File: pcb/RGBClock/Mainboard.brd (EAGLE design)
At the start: 99.8 x 70.1 mm, 106 parts, among them IC1 MCP23017SO, IC2 LT1763CS8-1.5, K1 G6K-2F, K2 G6K-2F, K3 G6K-2F, K4 G6K-2F, Q1 32.768KHz, U1 MAX6369KA+T, U10 NX3L1G384GW, U11 NX3L1G384GW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

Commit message: dab routed
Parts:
- moved C23 1.98 mm to (61.1, 17.5), flipped to the top, turned to 180 degrees
- moved C24 1.37 mm to (60.5, 21.5), flipped to the top
- moved C25 1.37 mm to (63.0, 21.5), flipped to the top
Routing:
- net N$69: track 5.35 -> 3.68 mm, vias 1 -> 0
- net N$34: track 5.85 -> 4.79 mm, vias 1 -> 0
- net N$27: track 8.59 -> 7.80 mm, vias 1 -> 0
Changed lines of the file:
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@@
 <attribute name="NAME" x="62.042" y="7.874" size="1.27" layer="26" rot="MR180"/>
 </element>
-<element name="C23" library="Mainboard" package="RCL_C0805" value="1u" x="62.672" y="16.256" smashed="yes" rot="MR0">
-<attribute name="NAME" x="63.942" y="17.526" size="1.27" layer="26" rot="MR0"/>
-</element>
-<element name="C24" library="Mainboard" package="RCL_C0805" value="8.2p" x="61.722" y="21.016" smashed="yes" rot="MR270">
-<attribute name="NAME" x="60.452" y="22.286" size="1.27" layer="26" rot="MR270"/>
-</element>
-<element name="C25" library="Mainboard" package="RCL_C0805" value="8.2p" x="64.262" y="21.016" smashed="yes" rot="MR270">
-<attribute name="NAME" x="62.992" y="22.286" size="1.27" layer="26" rot="MR270"/>
+<element name="C23" library="Mainboard" package="RCL_C0805" value="1u" x="61.148" y="17.526" smashed="yes" rot="R180">
+<attribute name="NAME" x="62.418" y="16.256" size="1.27" layer="25" rot="R180"/>
+</element>
+<element name="C24" library="Mainboard" package="RCL_C0805" value="8.2p" x="60.452" y="21.524" smashed="yes" rot="R270">
+<attribute name="NAME" x="61.722" y="22.794" size="1.27" layer="25" rot="R270"/>
+</element>
+<element name="C25" library="Mainboard" package="RCL_C0805" value="8.2p" x="62.992" y="21.524" smashed="yes" rot="R270">
+<attribute name="NAME" x="64.262" y="22.794" size="1.27" layer="25" rot="R270"/>
 </element>
 <element name="C11" library="Mainboard" package="RCL_C0805" value="8.2p" x="47.178" y="25.908" smashed="yes" rot="MR0">
@@
 <wire x1="43.18" y1="18.796" x2="64.546" y2="26.028" width="0" layer="19" extent="1-1"/>
 <wire x1="43.18" y1="17.526" x2="43.18" y2="18.796" width="0" layer="19" extent="1-1"/>
-<wire x1="64.262" y1="21.966" x2="64.546" y2="26.028" width="0" layer="19" extent="1-16"/>
-<wire x1="61.722" y1="21.966" x2="64.262" y2="21.966" width="0" layer="19" extent="16-16"/>
+<wire x1="62.992" y1="22.474" x2="64.546" y2="26.028" width="0" layer="19" extent="1-16"/>
+<wire x1="60.452" y1="22.474" x2="62.992" y2="22.474" width="0" layer="19" extent="16-16"/>
 <wire x1="39.37" y1="22.606" x2="43.18" y2="18.796" width="0" layer="19" extent="1-1"/>
 <wire x1="37.98" y1="18.796" x2="39.37" y2="22.606" width="0" layer="19" extent="1-1"/>
@@
 <wire x1="87.264" y1="28.956" x2="82.804" y2="31.308" width="0" layer="19" extent="1-1"/>
 <wire x1="87.7824" y1="27.051" x2="87.264" y2="28.956" width="0" layer="19" extent="1-1"/>
-<wire x1="63.622" y1="16.256" x2="64.262" y2="21.966" width="0" layer="19" extent="16-16"/>
+<wire x1="62.098" y1="17.526" x2="62.992" y2="22.474" width="0" layer="19" extent="16-16"/>
 <wire x1="87.122" y1="21.209" x2="87.7824" y2="27.051" width="0" layer="19" extent="1-1"/>
 <wire x1="84.948" y1="19.304" x2="87.122" y2="21.209" width="0" layer="19" extent="1-1"/>
 <wire x1="96.266" y1="25.356" x2="87.7824" y2="27.051" width="0" layer="19" extent="1-1"/>
-<wire x1="54.683" y1="14.532" x2="63.622" y2="16.256" width="0" layer="19" extent="1-16"/>
+<wire x1="54.683" y1="14.532" x2="62.098" y2="17.526" width="0" layer="19" extent="1-16"/>
 <wire x1="54.183" y1="14.532" x2="54.683" y2="14.532" width="0" layer="19" extent="1-1"/>
 <wire x1="53.683" y1="14.532" x2="54.183" y2="14.532" width="0" layer="19" extent="1-1"/>
@@
 <contactref element="TP3" pad="TP"/>
 <contactref element="C25" pad="2"/>
-<wire x1="56.708" y1="17.557" x2="58.959" y2="17.557" width="0.254" layer="1"/>
-<wire x1="58.959" y1="17.557" x2="59.436" y2="18.034" width="0.254" layer="1"/>
-<via x="59.436" y="18.034" extent="1-16" drill="0.6096"/>
-<wire x1="59.436" y1="18.034" x2="62.23" y2="18.034" width="0.254" layer="16"/>
-<wire x1="62.23" y1="18.034" x2="64.262" y2="20.066" width="0.254" layer="16"/>
-<wire x1="64.262" y1="20.066" x2="71.12" y2="17.018" width="0" layer="19" extent="1-16"/>
+<wire x1="62.992" y1="20.066" x2="61.976" y2="19.05" width="0.254" layer="1"/>
+<wire x1="62.992" y1="20.066" x2="62.992" y2="20.574" width="0.254" layer="1"/>
+<wire x1="56.708" y1="17.557" x2="57.627" y2="17.557" width="0.254" layer="1"/>
+<wire x1="59.138425" y1="19.05" x2="57.653425" y2="17.565" width="0.254" layer="1"/>
+<wire x1="61.976" y1="19.05" x2="59.138425" y2="19.05" width="0.254" layer="1"/>
+<wire x1="62.992" y1="20.574" x2="71.12" y2="17.018" width="0" layer="19" extent="1-1"/>
+<wire x1="57.627" y1="17.557" x2="57.653425" y2="17.565" width="0" layer="19" extent="1-1"/>
 <wire x1="75.9968" y1="9.2964" x2="71.12" y2="17.018" width="0" layer="19" extent="1-1"/>
 </signal>
@@
 <contactref element="C24" pad="2"/>
 <wire x1="56.708" y1="18.057" x2="57.427" y2="18.057" width="0.254" layer="1"/>
-<wire x1="57.427" y1="18.057" x2="58.42" y2="19.05" width="0.254" layer="1"/>
-<via x="58.42" y="19.05" extent="1-16" drill="0.6096"/>
-<wire x1="58.42" y1="19.05" x2="60.706" y2="19.05" width="0.254" layer="16"/>
-<wire x1="60.706" y1="19.05" x2="61.722" y2="20.066" width="0.254" layer="16"/>
+<wire x1="59.944" y1="20.574" x2="60.452" y2="20.574" width="0.254" layer="1"/>
+<wire x1="57.427" y1="18.057" x2="59.944" y2="20.574" width="0.254" layer="1"/>
 <wire x1="75.9968" y1="13.8684" x2="71.12" y2="18.796" width="0" layer="19" extent="1-1"/>
-<wire x1="61.722" y1="20.066" x2="71.12" y2="18.796" width="0" layer="19" extent="1-16"/>
+<wire x1="60.452" y1="20.574" x2="71.12" y2="18.796" width="0" layer="19" extent="1-1"/>
 </signal>
 <signal name="N$28">
@@
 <contactref element="C23" pad="2"/>
 <contactref element="U$2" pad="17"/>
-<wire x1="56.708" y1="17.057" x2="58.889" y2="17.057" width="0.254" layer="1"/>
-<wire x1="58.889" y1="17.057" x2="59.436" y2="16.51" width="0.254" layer="1"/>
-<via x="59.436" y="16.51" extent="1-16" drill="0.6096"/>
-<wire x1="59.436" y1="16.51" x2="61.468" y2="16.51" width="0.254" layer="16"/>
-<wire x1="61.468" y1="16.51" x2="61.722" y2="16.256" width="0.254" layer="16"/>
+<wire x1="60.071" y1="17.399" x2="60.198" y2="17.526" width="0.254" layer="1"/>
+<wire x1="56.708" y1="17.057" x2="59.729" y2="17.057" width="0.254" layer="1"/>
+<wire x1="59.729" y1="17.057" x2="60.071" y2="17.399" width="0.254" layer="1"/>
 </signal>
 <signal name="N$70" class="4">

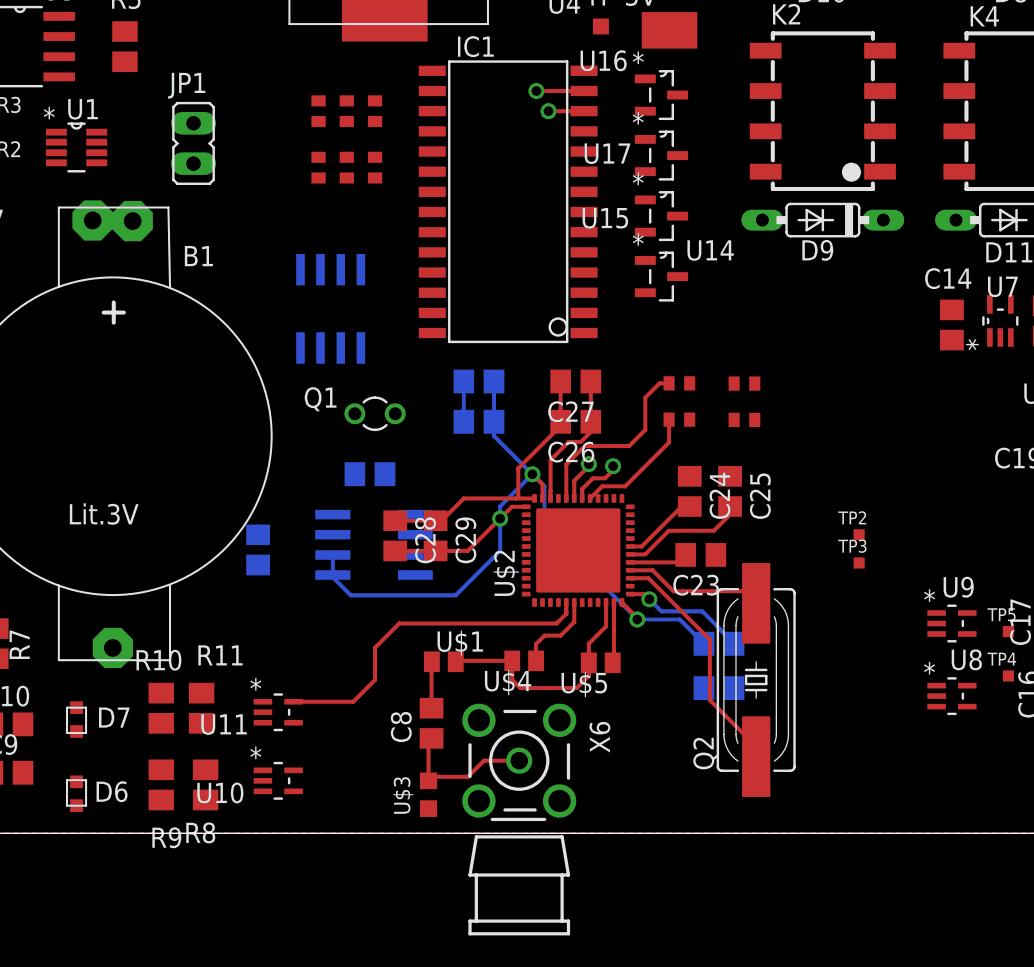
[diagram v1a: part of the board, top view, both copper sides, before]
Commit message: lower clearance to 6mil
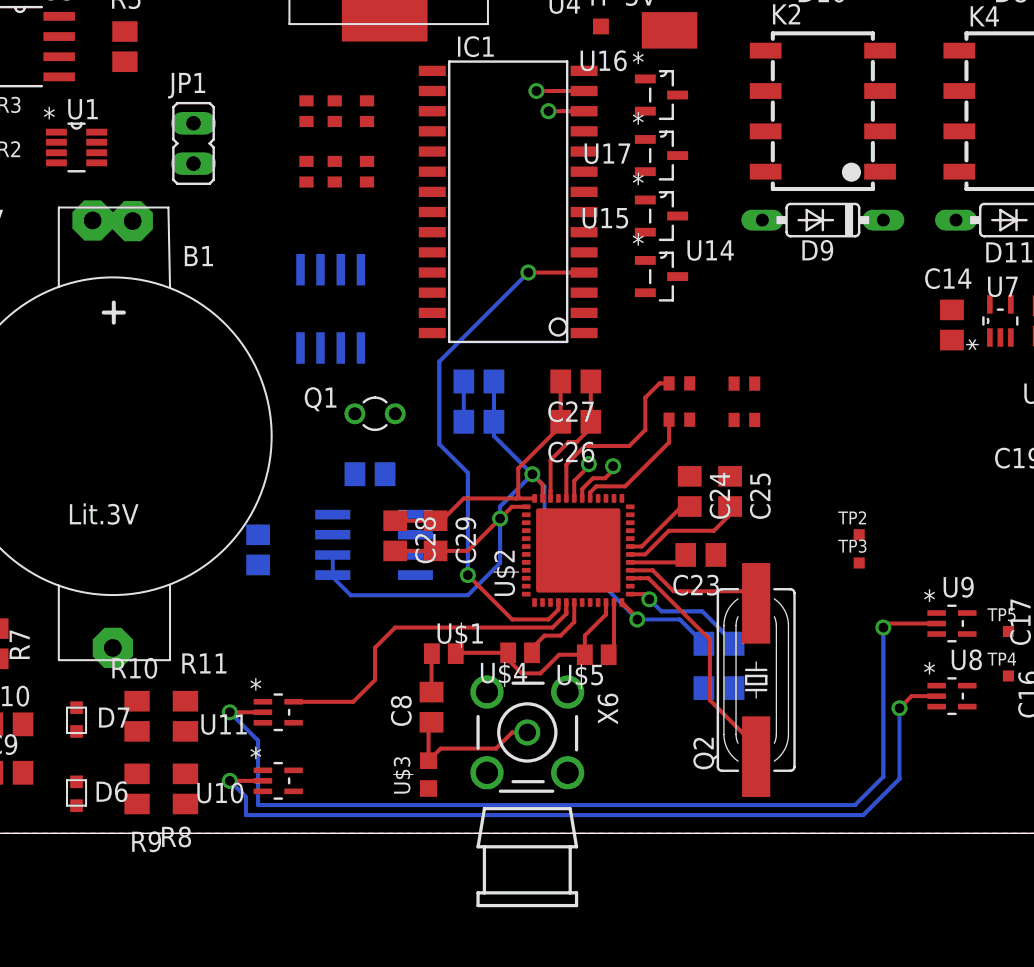
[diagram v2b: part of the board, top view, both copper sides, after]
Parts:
- moved R18 4.33 mm to (36.3, 41.7)
- moved R19 4.32 mm to (36.3, 45.5)
- moved R14 3.06 mm to (40.1, 41.7)
- moved R15 3.05 mm to (40.1, 45.5)
- moved X6 1.85 mm to (50.2, 6.35)
- moved R10 1.61 mm to (25.7, 7.37)
- moved R8 1.55 mm to (25.7, 2.79)
- moved R9 1.30 mm to (28.7, 2.79)
- moved U$3 1.27 mm to (44.0, 3.70)
- moved R11 1.14 mm to (28.7, 7.37)
- moved C8 1.02 mm to (44.2, 7.94)
- moved R16 0.80 mm to (38.1, 41.7)
- moved R17 0.76 mm to (38.1, 45.5)
- moved U$4 0.57 mm to (49.7, 11.4)
- moved U$5 0.57 mm to (54.5, 11.2)
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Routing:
- net N$30: track 0.00 -> 61.6 mm, vias 0 -> 2
- net N$29: track 0.00 -> 53.9 mm, vias 0 -> 2
- net N$35: track 0.00 -> 33.2 mm, vias 0 -> 2
- net N$59: track 15.2 -> 13.3 mm
- net N$61: track 2.94 -> 2.43 mm

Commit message: juiste positie
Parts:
- removed R20: A0-1, Mainboard:RESISTOR_R0402:1
- removed R21: A0-0, Mainboard:RESISTOR_R0402:1
- removed R22: A1-1, Mainboard:RESISTOR_R0402:1
- removed R24: A1-0, Mainboard:RESISTOR_R0402:1
- removed U$2: SI4684-A10, Mainboard:MAINBOARD_QFN48
- added U$6: SI4684-MYSMD, Mainboard:QFN48-SI4684
- moved C7 10.3 mm to (75.2, 25.4)
- moved U7 10.3 mm to (72.4, 25.4)
- moved C14 9.89 mm to (69.6, 25.4)
- moved TP3 8.30 mm to (74.2, 9.32)
- moved TP2 5.80 mm to (74.2, 13.9)
- moved C29 1.54 mm to (44.7, 20.3)
- moved C28 1.53 mm to (42.1, 20.3)
- moved C23 1.36 mm to (62.4, 17.9)
- moved Q2 1.31 mm to (65.1, 8.44)
- moved C22 1.14 mm to (61.3, 9.65)
- moved C5 1.05 mm to (60.2, 54.1)
- moved C12 1.05 mm to (61.3, 12.2)
- moved C11 1.00 mm to (47.2, 26.9)
- moved C26 1.00 mm to (53.3, 26.9)
- moved C4 0.92 mm to (33.9, 18.5)
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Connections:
- removed net N$14: R20.1, R21.2, U$2.32
- removed net N$65: R22.1, R24.2, U$2.29
- new net N$62: U$6.5
- net +1.8V: now also U$6.12, U$6.35, U$6.37; no longer U$2.12, U$2.35, U$2.37
- net +3V3: now also U$6.34; no longer R20.2, R22.2, U$2.34, U$2.5
- net GND: now also U$6.29, U$6.32, U$6.39, U$6.40, U$6.41, U$6.42, U$6.6, U$6.7, U$6.8, U$6.9; no longer R21.1, R24.1, U$2.39, U$2.40, U$2.41, U$2.42, U$2.6, U$2.7, U$2.8, U$2.9
- net N$2: now also U$6.15; no longer U$2.15
- net N$26: now also U$6.16; no longer U$2.16
- net N$27: now also U$6.18; no longer U$2.18
- net N$32: now also U$6.11; no longer U$2.11
- net N$34: now also U$6.19; no longer U$2.19
- net N$35: now also U$6.4; no longer U$2.4
- net N$59: now also U$6.10; no longer U$2.10
- net N$68: now also U$6.13; no longer U$2.13
- net N$69: now also U$6.17; no longer U$2.17
- net N$70: now also U$6.36; no longer U$2.36
- net SCL: now also U$6.30; no longer U$2.30
- net SDA: now also U$6.31; no longer U$2.31
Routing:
- net N$30: track 61.6 -> 0.00 mm, vias 2 -> 0
- net +1.8V: track 55.9 -> 0.00 mm, vias 3 -> 0
- net N$29: track 53.9 -> 0.00 mm, vias 2 -> 0
- net N$35: track 33.2 -> 0.00 mm, vias 2 -> 0
- net +3V3: track 30.4 -> 0.00 mm
- net N$70: track 19.9 -> 0.00 mm
- net N$2: track 14.2 -> 0.00 mm
- net N$59: track 13.3 -> 0.00 mm
- net N$14: track 11.9 -> 0.00 mm
- net N$28: track 9.45 -> 0.00 mm
- net N$26: track 8.86 -> 0.00 mm
- net N$65: track 8.27 -> 0.00 mm
- net N$68: track 7.85 -> 0.00 mm, vias 1 -> 0
- net N$27: track 7.80 -> 0.00 mm
- net SDA: track 5.54 -> 0.00 mm, vias 2 -> 0
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
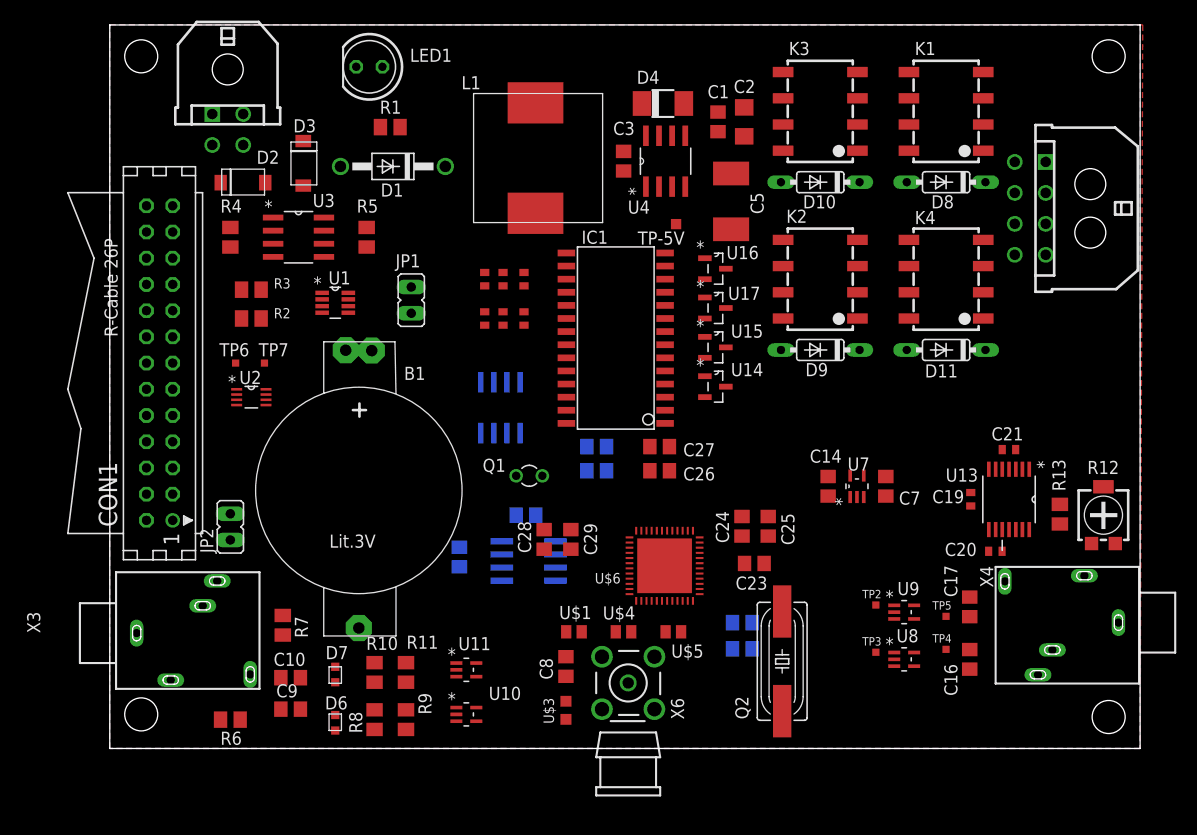
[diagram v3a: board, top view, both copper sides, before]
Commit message: met kleiner kristal
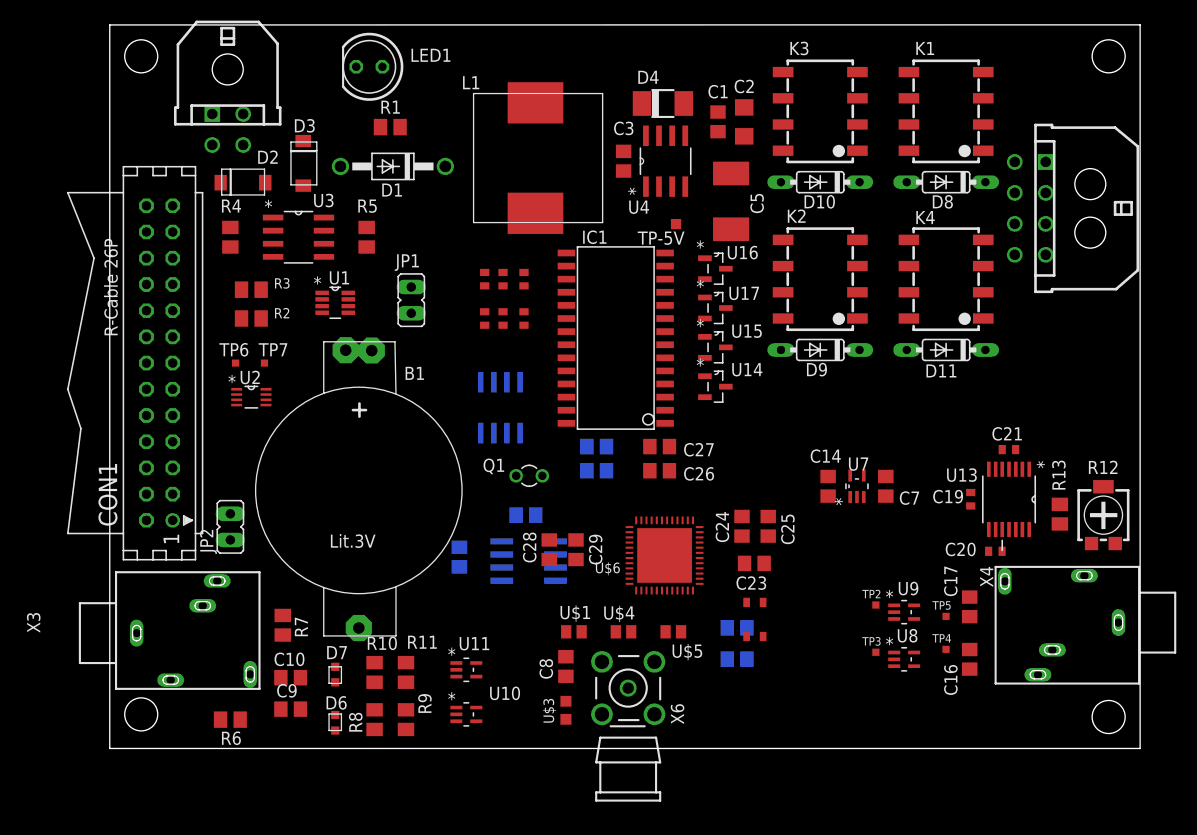
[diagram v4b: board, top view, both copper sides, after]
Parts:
- removed Q2: (no value), Mainboard:MAINBOARD_CRYSTAL_SM49
- added U$2: ABM8-CRYSTAL, Mainboard:ABM8
- moved C22 1.12 mm to (60.8, 8.65)
- moved C28 1.12 mm to (42.6, 19.3)
- moved C29 1.12 mm to (45.2, 19.3)
- moved U$6 1.00 mm to (53.8, 18.7)
- moved C12 0.71 mm to (60.8, 11.7)
- moved X6 0.50 mm to (50.2, 5.85)
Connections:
- net GND: now also U$2.2, U$2.4
- net N$2: now also U$2.1; no longer Q2.1
- net N$26: now also U$2.3; no longer Q2.2
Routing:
- removed copper zone on layer 1, net GND
- removed copper zone on layer 16, net GND

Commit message: move dab
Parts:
- moved U$6 1.00 mm to (53.8, 17.7)

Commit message: routed
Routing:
- net GND: track 0.00 -> 614.4 mm, vias 0 -> 10
- net +3V3: track 0.00 -> 243.0 mm, vias 0 -> 1
- net +5V: track 0.00 -> 166.7 mm
- net VCC: track 0.00 -> 143.6 mm
- net SDA: track 0.00 -> 99.5 mm, vias 0 -> 4
- net SCL: track 0.00 -> 92.6 mm, vias 0 -> 3
- net +1.8V: track 0.00 -> 62.8 mm, vias 0 -> 3
- net N$30: track 0.00 -> 58.3 mm, vias 0 -> 2
- net N$29: track 0.00 -> 56.6 mm
- net N$66: track 0.00 -> 49.0 mm, vias 0 -> 2
- net N$38: track 0.00 -> 46.6 mm, vias 0 -> 2
- net N$33: track 0.00 -> 41.6 mm, vias 0 -> 2
- net N$31: track 0.00 -> 41.1 mm
- net N$53: track 0.00 -> 36.3 mm
- net N$36: track 0.00 -> 36.3 mm
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- added copper zone on layer 1, net GND
- added copper zone on layer 16, net GND
